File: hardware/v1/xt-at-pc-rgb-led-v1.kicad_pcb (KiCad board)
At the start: 2 copper layers, 48 x 22.5 mm, 18 parts, among them J1 PLED, J2 HDD, J3 TURBO, J4 RGB LED (A R G B), J5 SW IN, J6 SW OUT, Q1 BC547, Q2 BC547

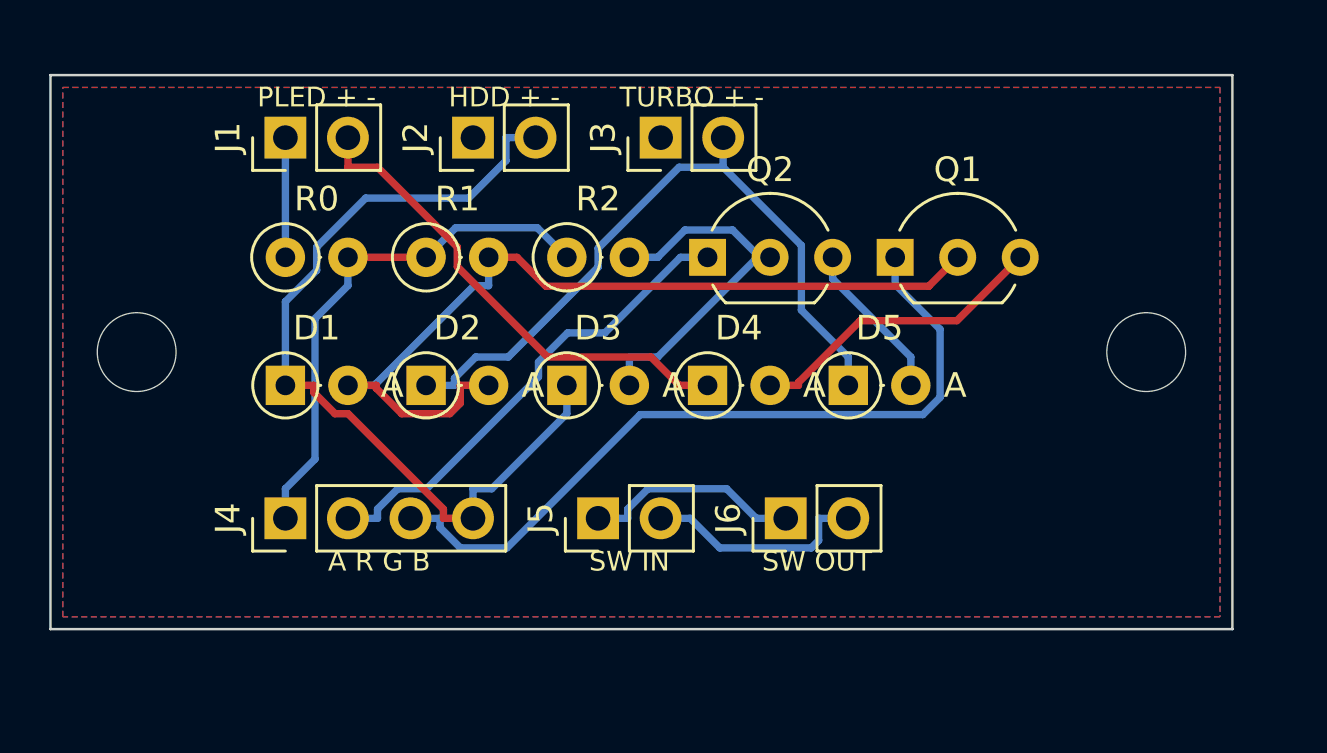
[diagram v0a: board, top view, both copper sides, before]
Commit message: Lay resistors and diodes flat on both boards
7.62 mm horizontal footprints, side by side; mounting holes in gaps
between the parts. v1 44 x 25.5 mm, v2 42 x 36.4 mm. Component height
about 8.5 mm.

Co-Authored-By: Claude Opus 5.5 (1M context) <noreply@anthropic.com>
Claude-Session: https://claude.ai/code/session_01JRatMm8Q7Nvo5CN8dD4gBk
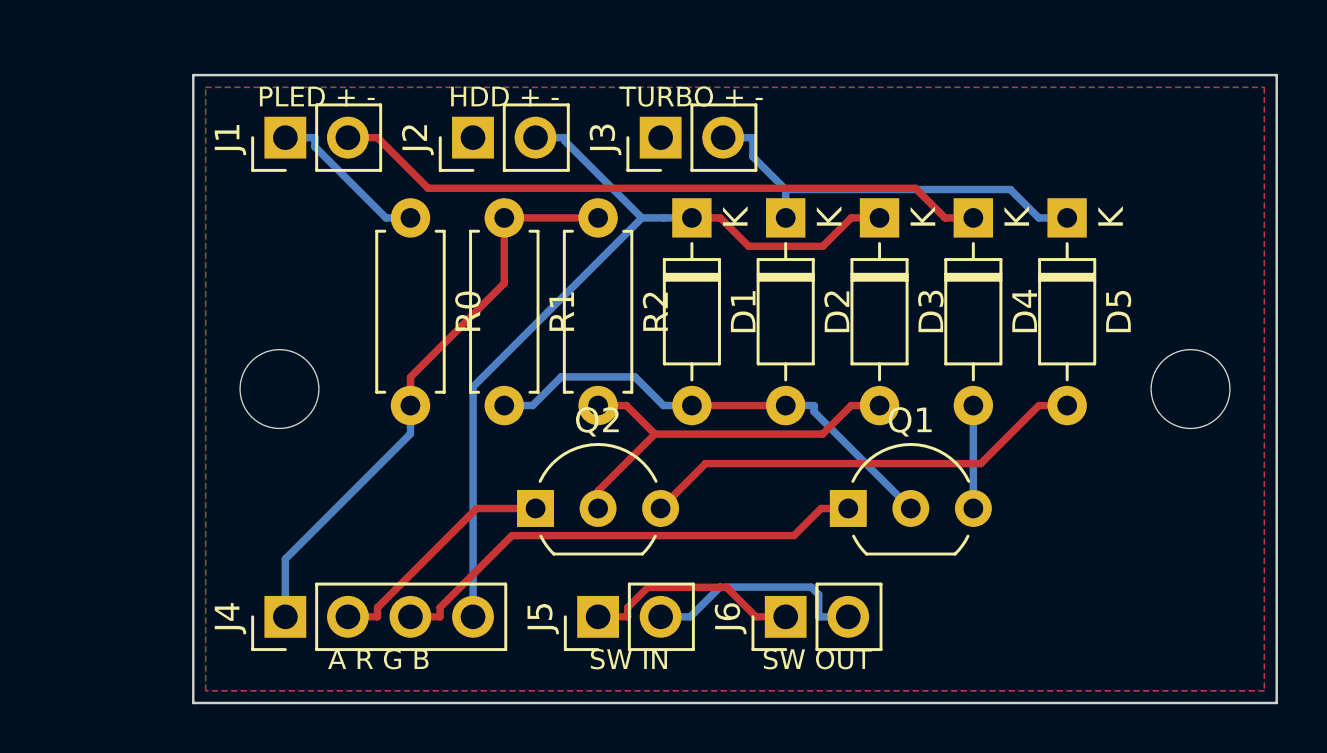
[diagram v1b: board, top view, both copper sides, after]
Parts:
- D1, D2, D3, D4, D5: footprint Diode_THT:D_DO-35_SOD27_P2.54mm_Vertical_AnodeUp -> Diode_THT:D_DO-35_SOD27_P7.62mm_Horizontal
- R0, R1, R2: footprint Resistor_THT:R_Axial_DIN0207_L6.3mm_D2.5mm_P2.54mm_Vertical -> Resistor_THT:R_Axial_DIN0207_L6.3mm_D2.5mm_P7.62mm_Horizontal
- moved D1 17.9 mm to (119.0, 105.8), turned to -90 degrees
- moved D2 16.1 mm to (122.9, 105.8), turned to -90 degrees
- moved D3 14.4 mm to (126.7, 105.8), turned to -90 degrees
- moved D4 12.8 mm to (130.5, 105.8), turned to -90 degrees
- moved Q2 12.4 mm to (112.7, 117.6)
- moved D5 11.2 mm to (134.3, 105.8), turned to -90 degrees
- moved Q1 10.4 mm to (125.4, 117.6)
- moved H1 5.99 mm to (102.3, 112.8)
- moved R0 5.33 mm to (107.6, 105.8), turned to -90 degrees
- moved J4 4.00 mm to (102.5, 122.0)
- moved J5 4.00 mm to (115.2, 122.0)
- moved J6 4.00 mm to (122.9, 122.0)
- moved R1 3.56 mm to (111.4, 105.8), turned to -90 degrees
- moved H2 2.34 mm to (139.3, 112.8)
- moved R2 2.04 mm to (115.2, 105.8), turned to -90 degrees
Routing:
- net /X1: track 35.8 -> 19.4 mm
- net /E2: track 6.52 -> 18.2 mm
- net /TURBO: track 28.5 -> 16.9 mm
- net /GREEN_K: track 31.2 -> 19.8 mm
- net /RED_K: track 19.6 -> 9.66 mm
- net /E1: track 12.4 -> 4.18 mm
- net GND: track 19.9 -> 26.8 mm
- net /ANODE: track 21.5 -> 23.7 mm
- net /PLED_P: track 4.86 -> 6.65 mm
- net /X2: track 14.7 -> 16.4 mm
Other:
- board size 48 x 22.5 mm -> 44 x 25.5 mm

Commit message: More margin above the top labels
1 mm more board above the connector labels so the silkscreen fits;
v1 44 x 26.5 mm, v2 42 x 38.4 mm (holes stay centred).

Co-Authored-By: Claude Opus 5.5 (1M context) <noreply@anthropic.com>
Claude-Session: https://claude.ai/code/session_01JRatMm8Q7Nvo5CN8dD4gBk
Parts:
- moved H1 0.50 mm to (102.3, 112.2)
- moved H2 0.50 mm to (139.3, 112.2)
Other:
- board size 44 x 25.5 mm -> 44 x 26.5 mm

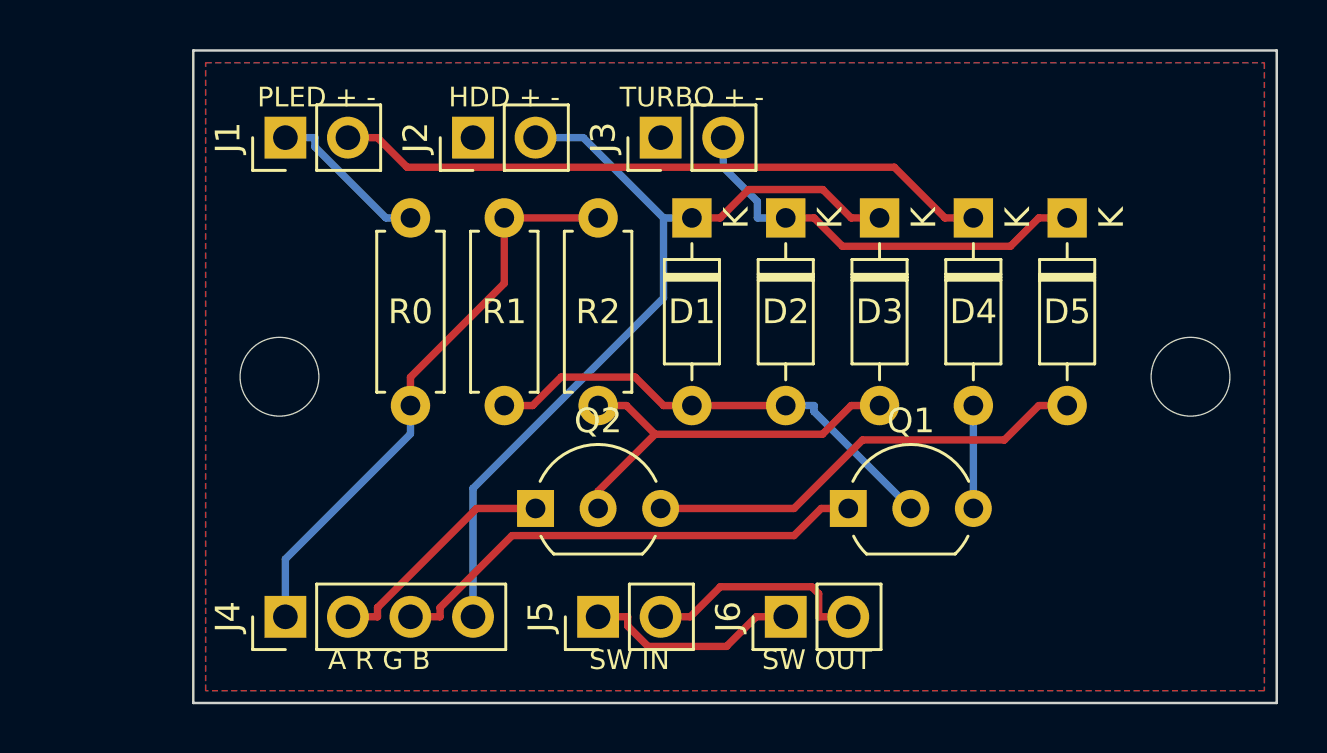
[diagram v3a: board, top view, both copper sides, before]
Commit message: v2: more margin, lower bottom labels; references along the parts
v2 42 x 40.4 mm: 1 mm more above the top labels, bottom connector
labels 2 mm lower. Resistor and diode references run along the body
on both boards.

Co-Authored-By: Claude Opus 5.5 (1M context) <noreply@anthropic.com>
Claude-Session: https://claude.ai/code/session_01JRatMm8Q7Nvo5CN8dD4gBk
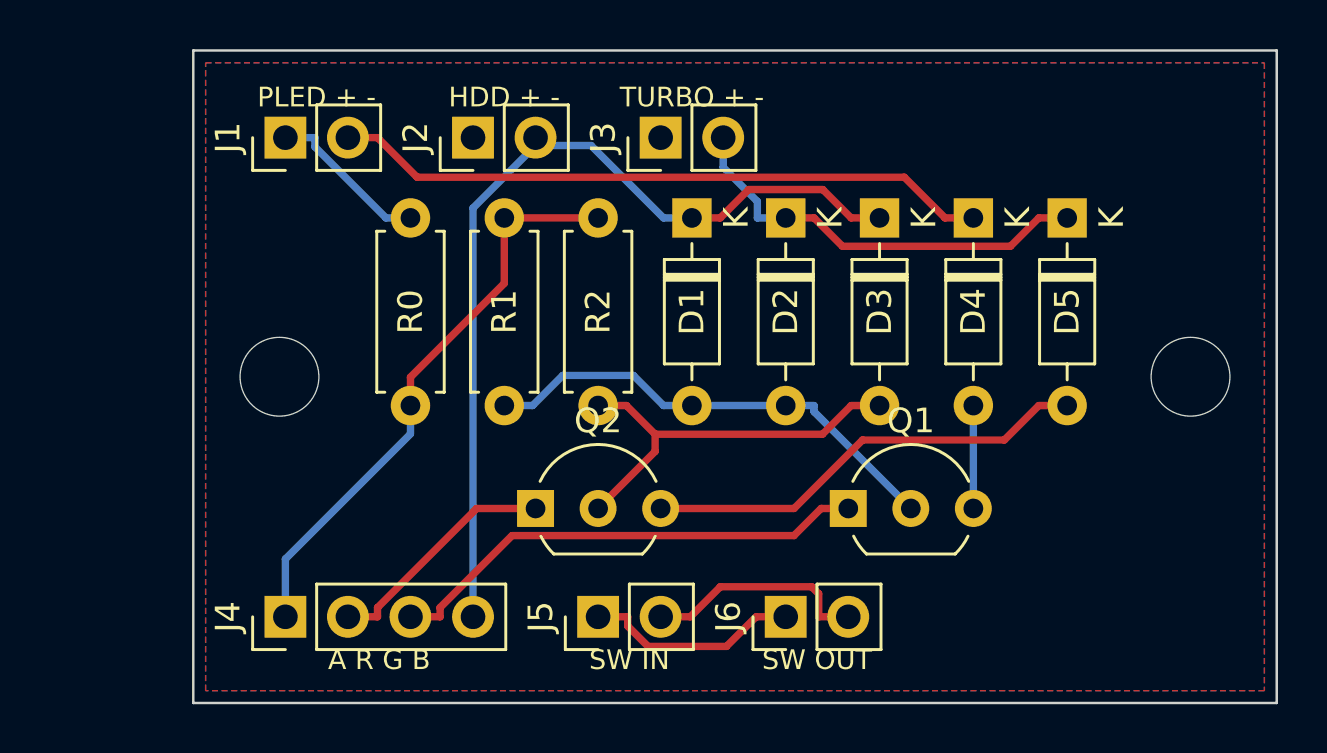
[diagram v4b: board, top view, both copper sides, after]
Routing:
- net /HDD: track 35.7 -> 36.7 mm
